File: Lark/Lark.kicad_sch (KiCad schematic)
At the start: 0 parts

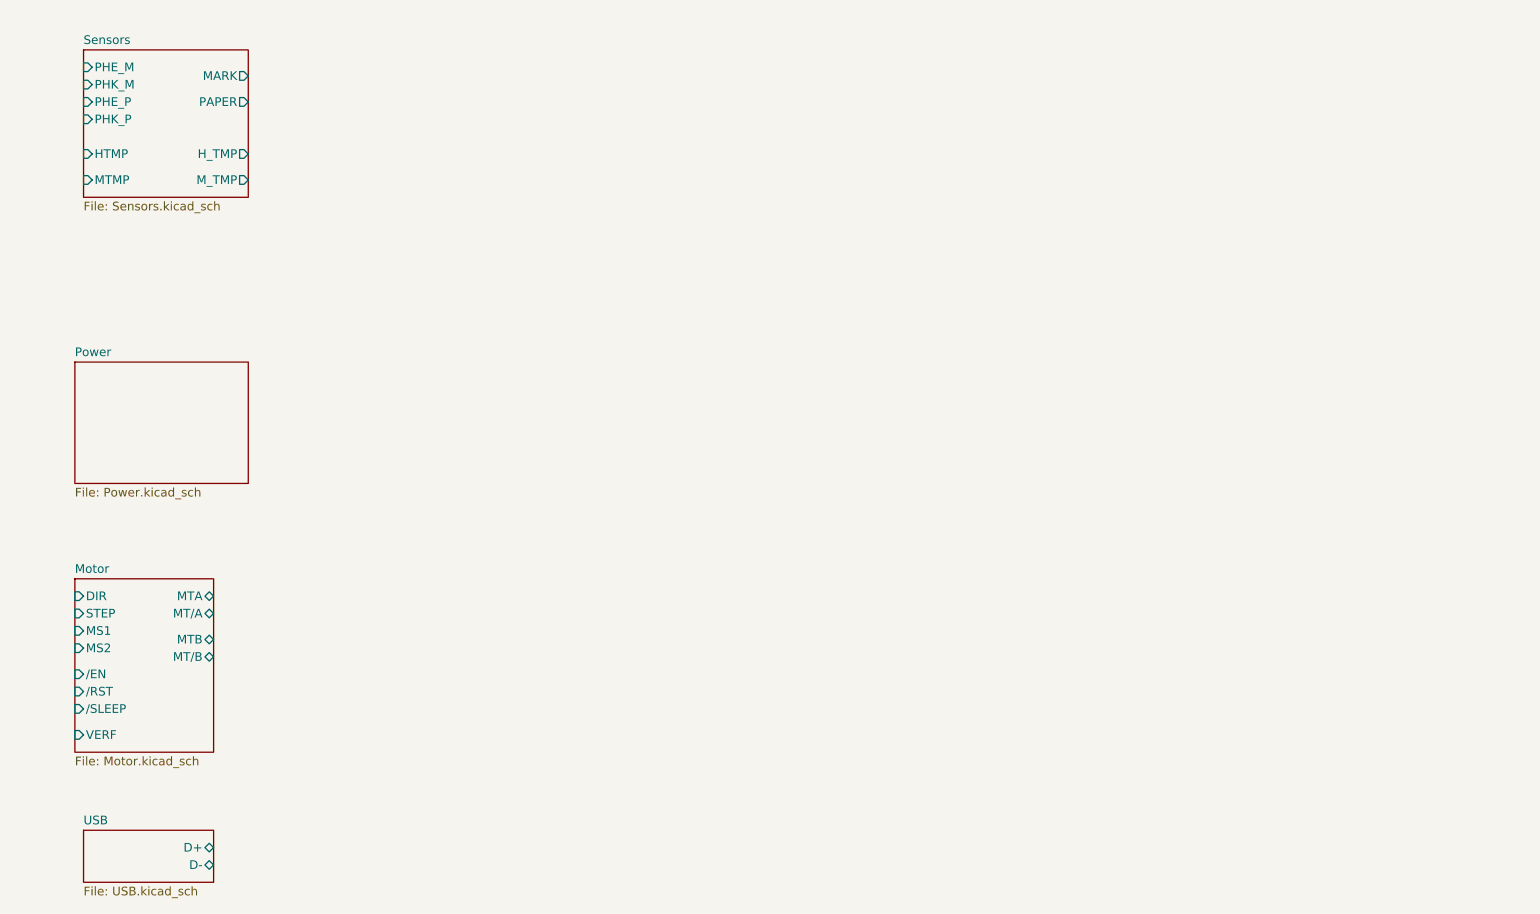
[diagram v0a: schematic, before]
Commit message: still porting design over from 'other' cad software.
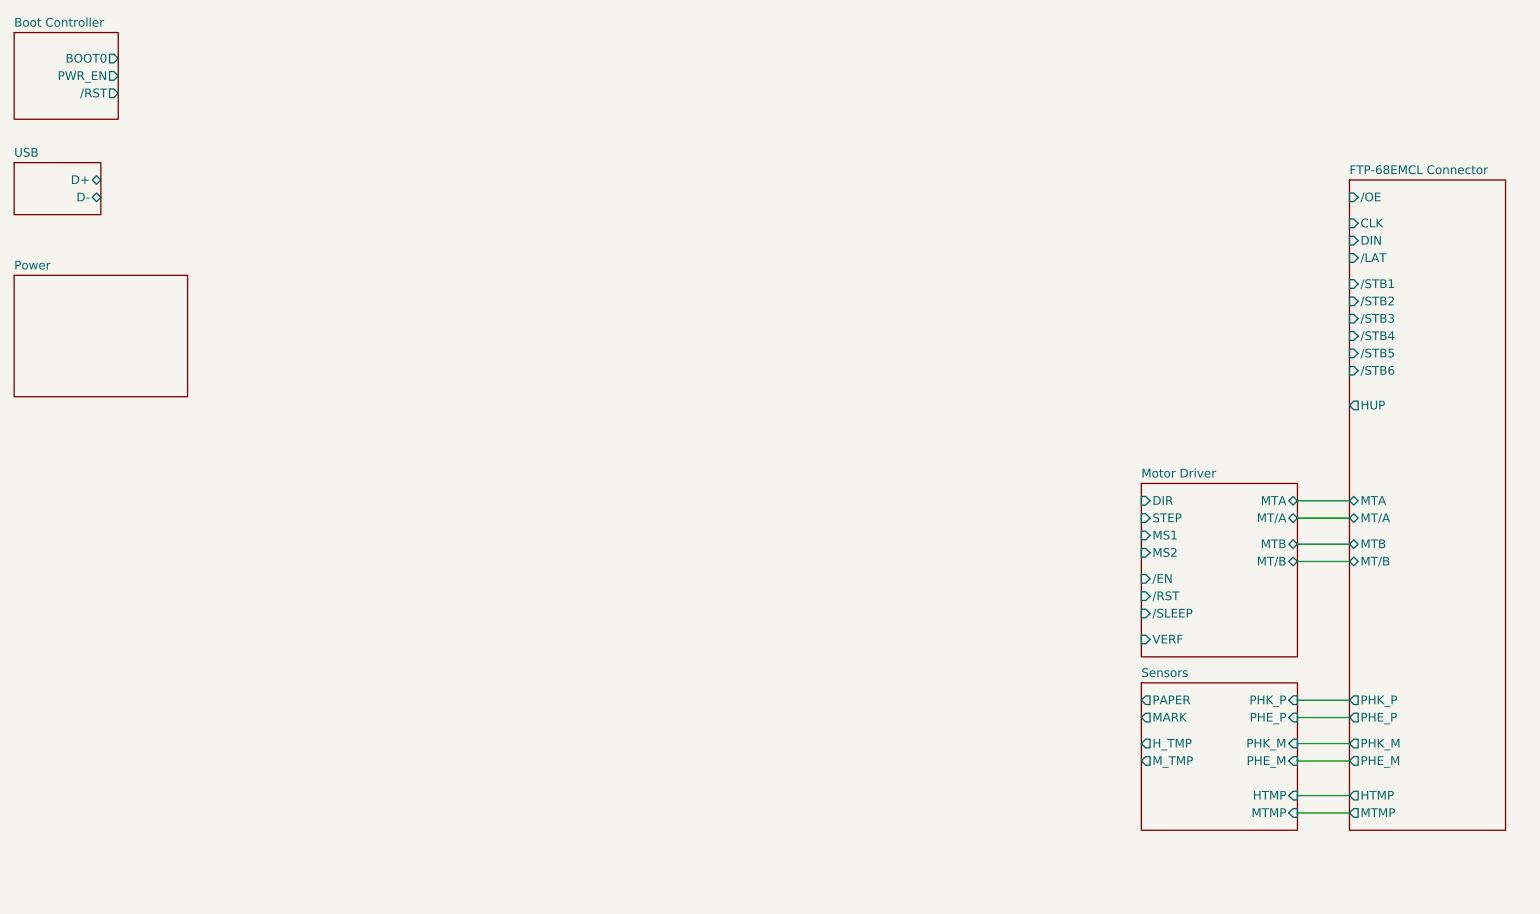
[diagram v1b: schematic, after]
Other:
- sheet Motor renamed Motor Driver
- added sheet Boot Controller (Boot_Controller.kicad_sch)
- added sheet FTP-68EMCL Connector (FTP-68EMCL_Connector.kicad_sch)
- sheet Motor Driver: file Motor.kicad_sch -> Motor_Driver.kicad_sch

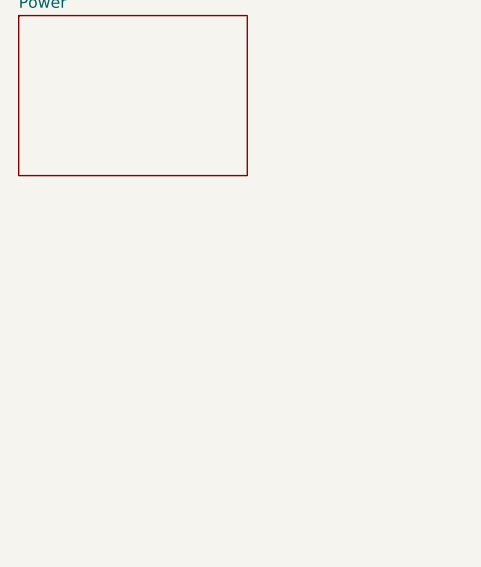
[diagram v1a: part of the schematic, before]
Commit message: Added Front pannel IO Sheet
- added new Molex connector to project lib.
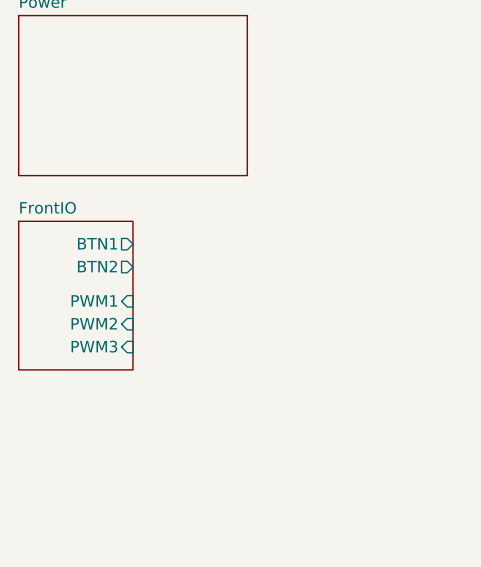
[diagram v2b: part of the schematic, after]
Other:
- added sheet FrontIO (FrontIO.kicad_sch)
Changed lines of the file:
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@@
+	)
+	(sheet
+		(at 17.78 76.2)
+		(size 12.7 16.51)
+		(exclude_from_sim no)
+		(in_bom yes)
+		(on_board yes)
+		(dnp no)
+		(fields_autoplaced yes)
+		(stroke
+			(width 0.1524)
+			(type solid)
+		)
+		(fill
+			(color 217 255 208 1.0000)
+		)
+		(property "Sheetname" "FrontIO"
+			(at 17.78 75.4884 0)
+			(effects
+				(font
+					(size 1.27 1.27)
+				)
+				(justify left bottom)
+			)
+		)
+		(property "Sheetfile" "FrontIO.kicad_sch"
+			(at 17.78 93.2946 0)
+			(effects
+				(font
+					(size 1.27 1.27)
+				)
+				(justify left top)
+				(hide yes)
+			)
+		)
+		(pin "BTN1" output
+			(at 30.48 78.74 0)
+			(effects
+				(font
+					(size 1.27 1.27)
+				)
+				(justify right)
+			)
+		)
+		(pin "BTN2" output
+			(at 30.48 81.28 0)
+			(effects
+				(font
+					(size 1.27 1.27)
+				)
+				(justify right)
+			)
+		)
+		(pin "PWM1" input
+			(at 30.48 85.09 0)
+			(effects
+				(font
+					(size 1.27 1.27)
+				)
+				(justify right)
+			)
+		)
+		(pin "PWM2" input
+			(at 30.48 87.63 0)
+			(effects
+				(font
+					(size 1.27 1.27)
+				)
+				(justify right)
+			)
+		)
+		(pin "PWM3" input
+			(at 30.48 90.17 0)
+			(effects
+				(font
+					(size 1.27 1.27)
+				)
+				(justify right)
+			)
+		)
+		(instances
+			(project "Lark"
+				(path "/a351af57-4353-47da-9f45-7393de572768"
+					(page "10")
+				)
+			)
+		)
 	)
 	(sheet

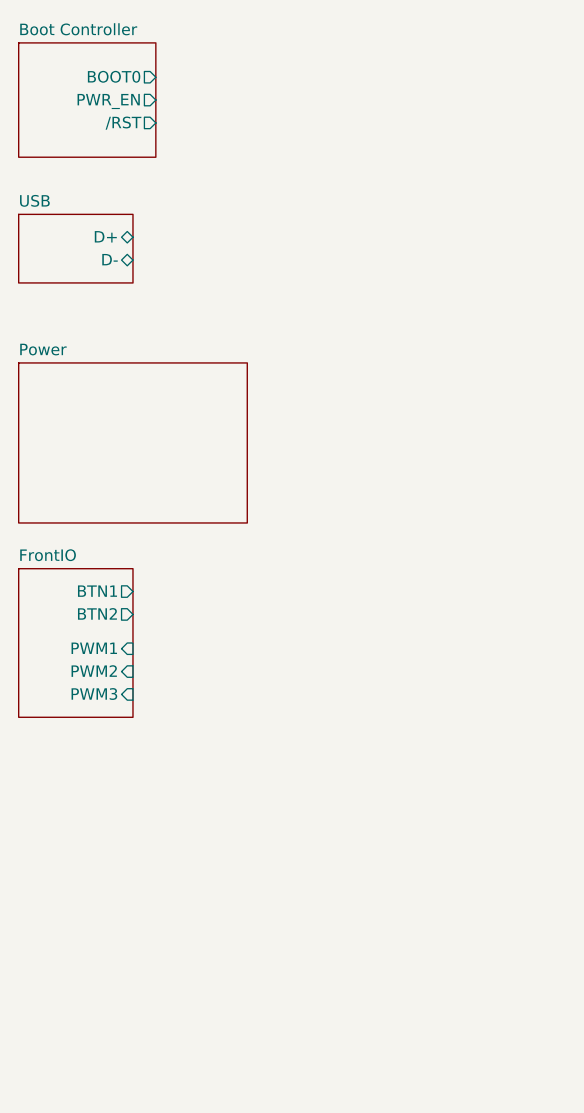
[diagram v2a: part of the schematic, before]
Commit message: added power section to schematic
It needs revised, due to thermal issue. Specifically in regards to my soft start circuit, the mosfet wont be able to handle the power dissipated during a slow turn on.
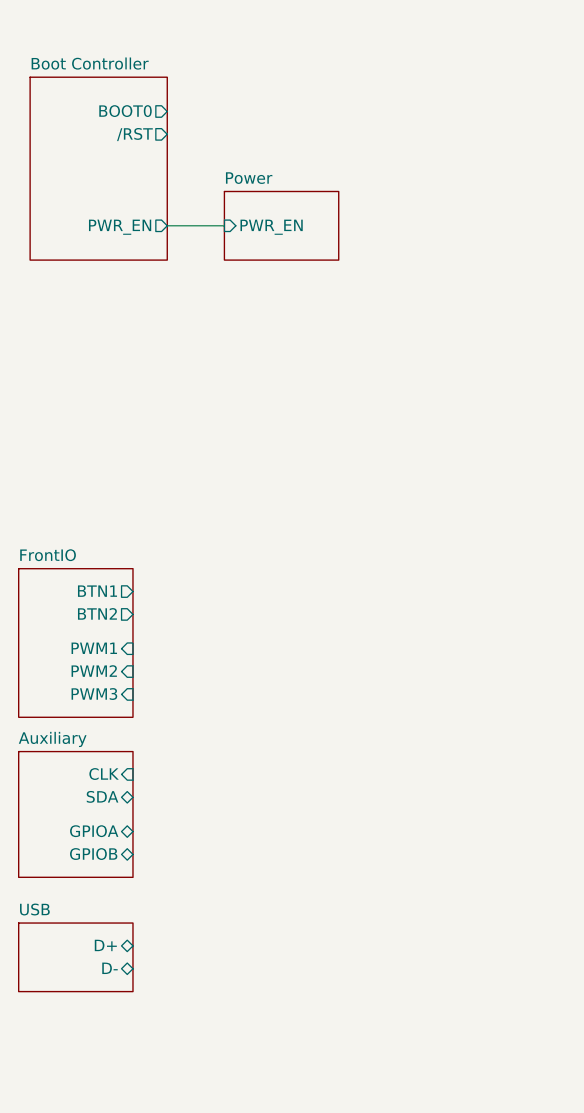
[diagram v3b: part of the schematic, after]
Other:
- added sheet Auxiliary (Auxiliary.kicad_sch)
- sheet Power ports: added PWR_EN; removed none
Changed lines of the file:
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@@
+		)
+	)
+	(wire
+		(pts
+			(xy 34.29 38.1) (xy 40.64 38.1)
+		)
+		(stroke
+			(width 0)
+			(type default)
 		)
 	)
@@
 	)
 	(sheet
-		(at 17.78 36.83)
+		(at 17.78 115.57)
 		(size 12.7 7.62)
 		(exclude_from_sim no)
@@
 		)
 		(property "Sheetname" "USB"
-			(at 17.78 36.1184 0)
+			(at 17.78 114.8584 0)
 			(effects
 				(font
@@
 		)
 		(property "Sheetfile" "USB.kicad_sch"
-			(at 17.78 45.0346 0)
+			(at 17.78 123.7746 0)
 			(effects
 				(font
@@
 		)
 		(pin "D+" bidirectional
-			(at 30.48 39.37 0)
+			(at 30.48 118.11 0)
 			(effects
 				(font
@@
 		)
 		(pin "D-" bidirectional
-			(at 30.48 41.91 0)
+			(at 30.48 120.65 0)
 			(effects
 				(font
@@
 	)
 	(sheet
-		(at 17.78 53.34)
-		(size 25.4 17.78)
+		(at 40.64 34.29)
+		(size 12.7 7.62)
 		(exclude_from_sim no)
 		(in_bom yes)
@@
 		)
 		(property "Sheetname" "Power"
-			(at 17.78 52.6284 0)
+			(at 40.64 33.5784 0)
 			(effects
 				(font
@@
 		)
 		(property "Sheetfile" "Power.kicad_sch"
-			(at 17.78 71.7046 0)
+			(at 40.64 42.4946 0)
 			(effects
 				(font
@@
 				(justify left top)
 				(hide yes)
+			)
+		)
+		(pin "PWR_EN" input
+			(at 40.64 38.1 180)
+			(effects
+				(font
+					(size 1.27 1.27)
+				)
+				(justify left)
 			)
 		)
@@
 	)
 	(sheet
-		(at 17.78 17.78)
-		(size 15.24 12.7)
+		(at 19.05 21.59)
+		(size 15.24 20.32)
 		(exclude_from_sim no)
 		(in_bom yes)
@@
 		)
 		(property "Sheetname" "Boot Controller"
-			(at 17.78 17.0684 0)
+			(at 19.05 20.8784 0)
 			(effects
 				(font
@@
 		)
 		(property "Sheetfile" "Boot_Controller.kicad_sch"
-			(at 17.78 31.0646 0)
+			(at 19.05 42.4946 0)
 			(effects
 				(font
@@
 		)
 		(pin "BOOT0" output
-			(at 33.02 21.59 0)
+			(at 34.29 25.4 0)
 			(effects
 				(font
@@
 		)
 		(pin "{slash}RST" output
-			(at 33.02 26.67 0)
+			(at 34.29 27.94 0)
 			(effects
 				(font
@@
 		)
 		(pin "PWR_EN" output
-			(at 33.02 24.13 0)
+			(at 34.29 38.1 0)
 			(effects
 				(font
@@
 				)
 			)
+		)
+	)
+	(sheet
+		(at 17.78 96.52)
+		(size 12.7 13.97)
+		(exclude_from_sim no)
+		(in_bom yes)
+		(on_board yes)
+		(dnp no)
+		(fields_autoplaced yes)
+		(stroke
+			(width 0.1524)
+			(type solid)
+		)
+		(fill
+			(color 217 255 208 1.0000)
+		)
+		(property "Sheetname" "Auxiliary"
+			(at 17.78 95.8084 0)
+			(effects
+				(font
+					(size 1.27 1.27)
+				)
+				(justify left bottom)
+			)
+		)
+		(property "Sheetfile" "Auxiliary.kicad_sch"
+			(at 17.78 111.0746 0)
+			(effects
+				(font
+					(size 1.27 1.27)
+				)
+				(justify left top)
+				(hide yes)
+			)
+		)
+		(pin "CLK" input
+			(at 30.48 99.06 0)
+			(effects
+				(font
+					(size 1.27 1.27)
+				)
+				(justify right)
+			)
+		)
+		(pin "SDA" bidirectional
+			(at 30.48 101.6 0)
+			(effects
+				(font
+					(size 1.27 1.27)
+				)
+				(justify right)
+			)
+		)
+		(pin "GPIOA" bidirectional
+			(at 30.48 105.41 0)
+			(effects
+				(font
+					(size 1.27 1.27)
+				)
+				(justify right)
+			)
+		)
+		(pin "GPIOB" bidirectional
+			(at 30.48 107.95 0)
+			(effects
+				(font
+					(size 1.27 1.27)
+				)
+				(justify right)
+			)
+		)
+		(instances
+			(project "Lark"
+				(path "/a351af57-4353-47da-9f45-7393de572768"
+					(page "11")
+				)
+			)

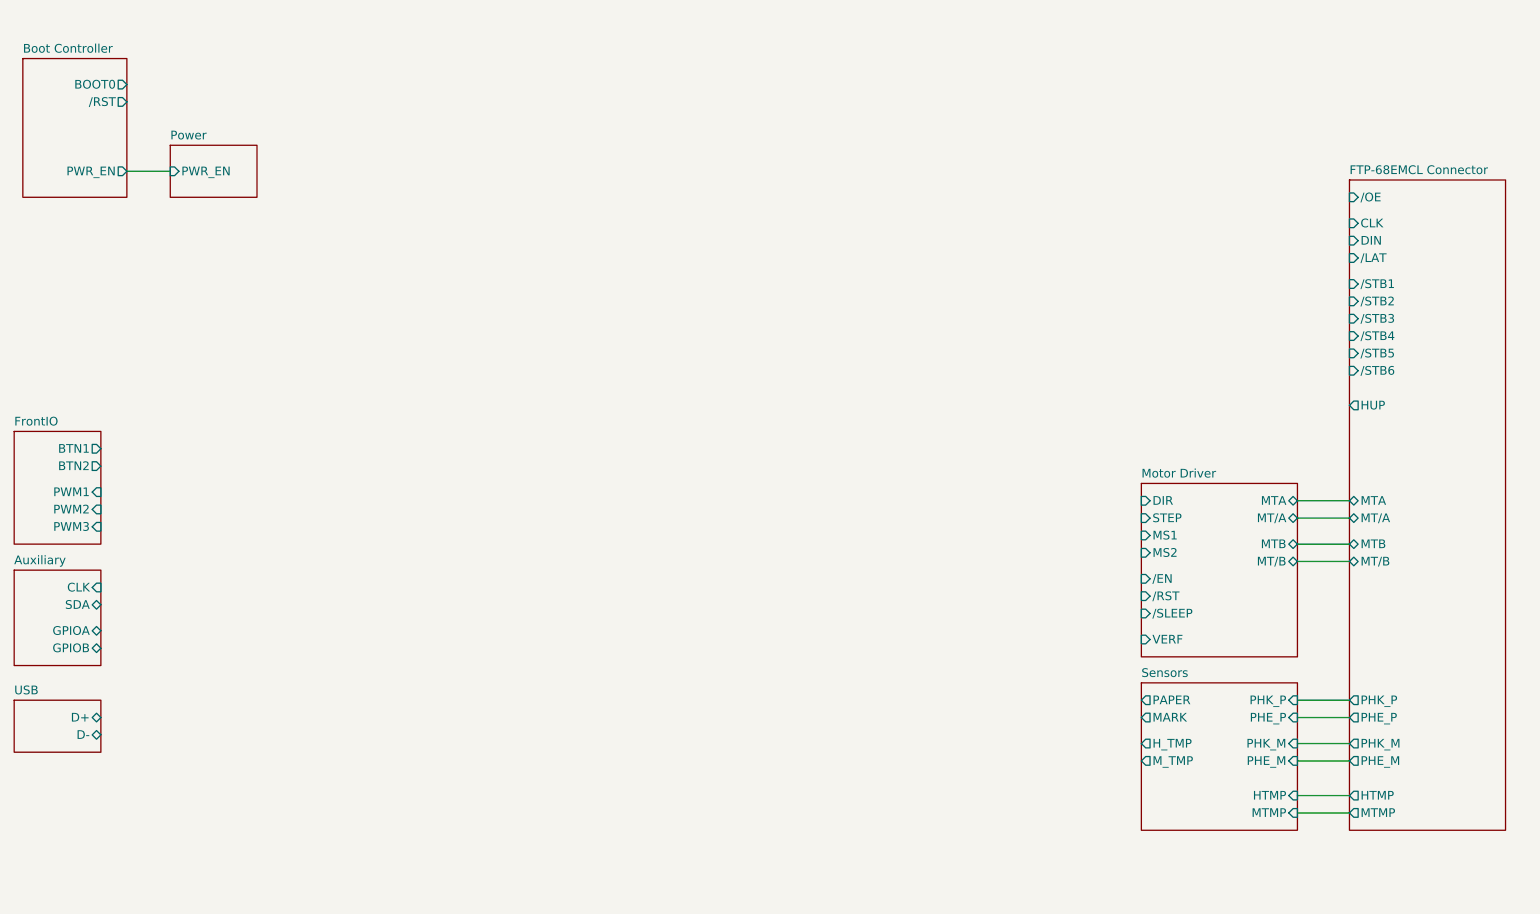
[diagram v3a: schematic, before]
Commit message: update, WIP
- Reannotated schematic.
- Added STM32 device.
- Fixed High-side switch (removed soft-start cap for device safety).
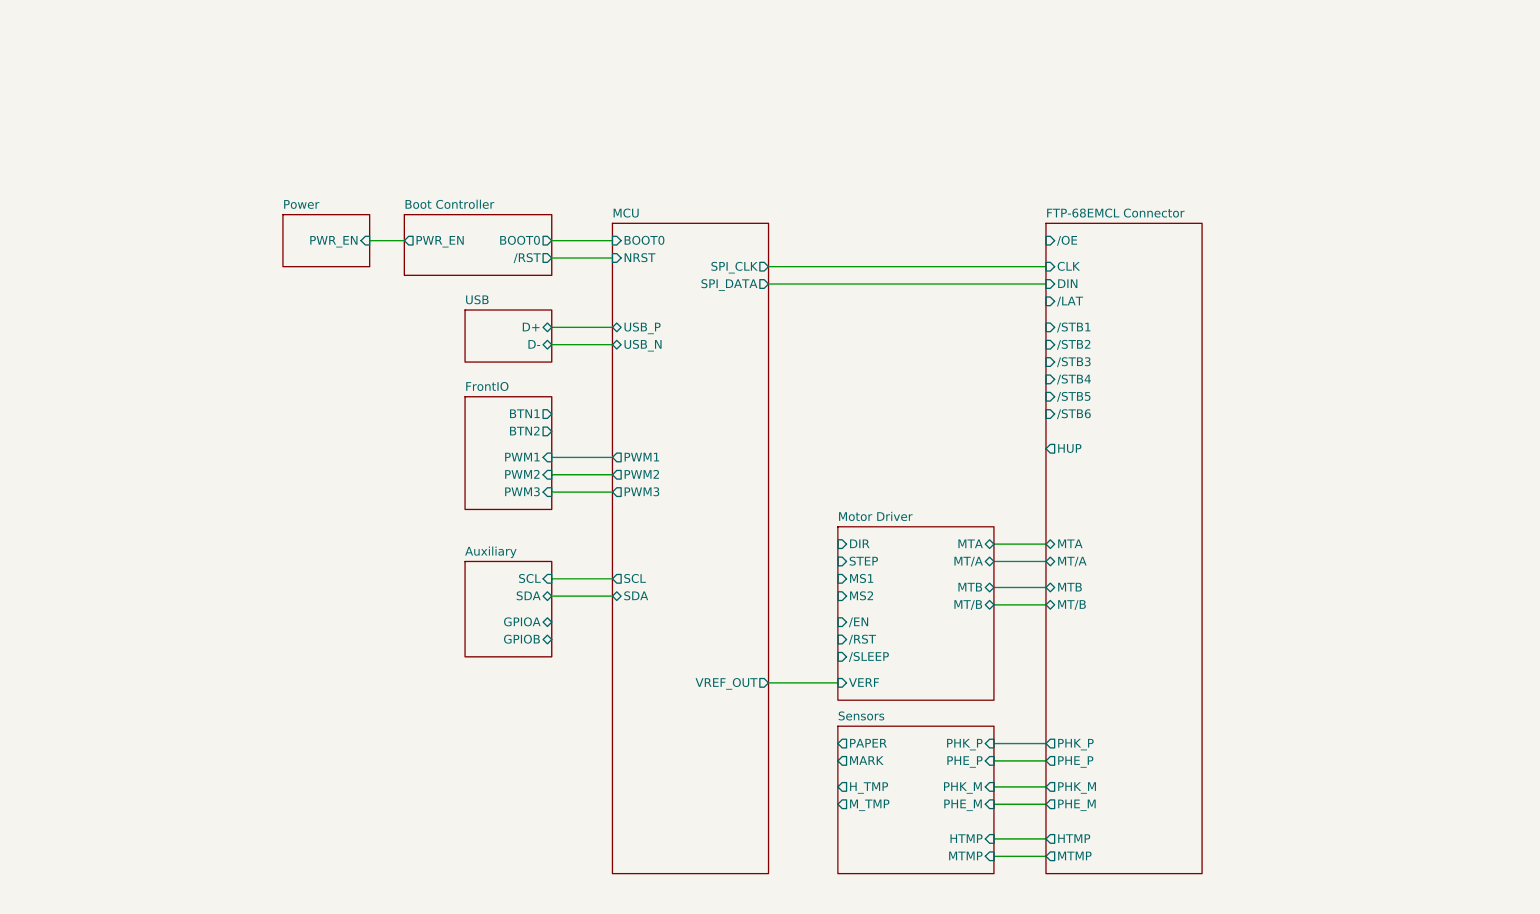
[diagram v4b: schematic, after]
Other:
- added sheet MCU (MCU.kicad_sch)
- sheet Auxiliary ports: added SCL; removed CLK
